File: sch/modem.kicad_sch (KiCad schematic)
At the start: 35 parts, among them J10 20579-001E, J11 732511150, J12 732511150, J13 732511150, J14 732511150, J6 20579-001E, J7 20579-001E, J8 20579-001E, J9 M.2_Socket_B, P1 SF72S006VBDR2500, Q3 NX3008NBKW_115

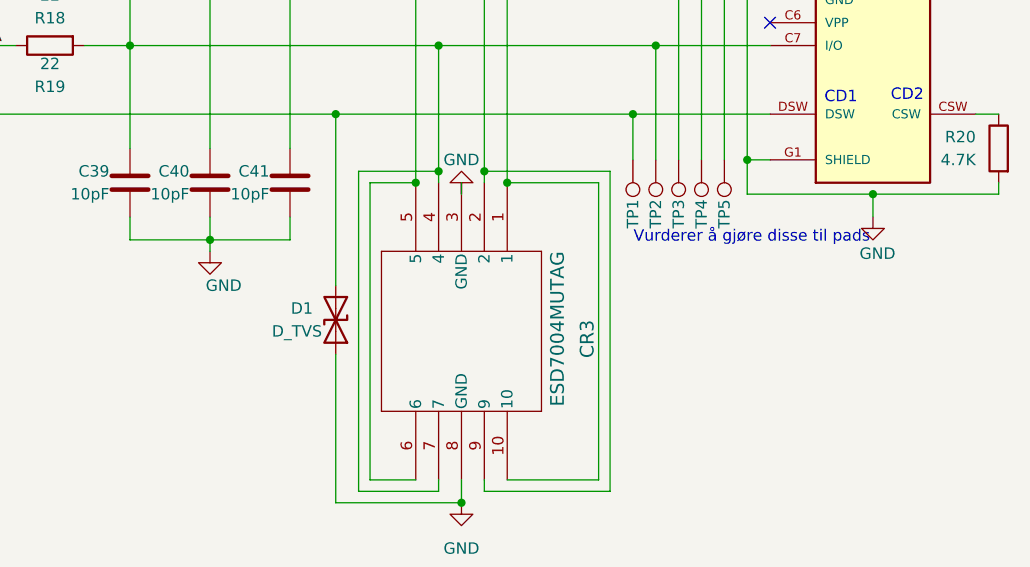
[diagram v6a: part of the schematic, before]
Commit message: partnumber, manufaturerer and description cleanup completed
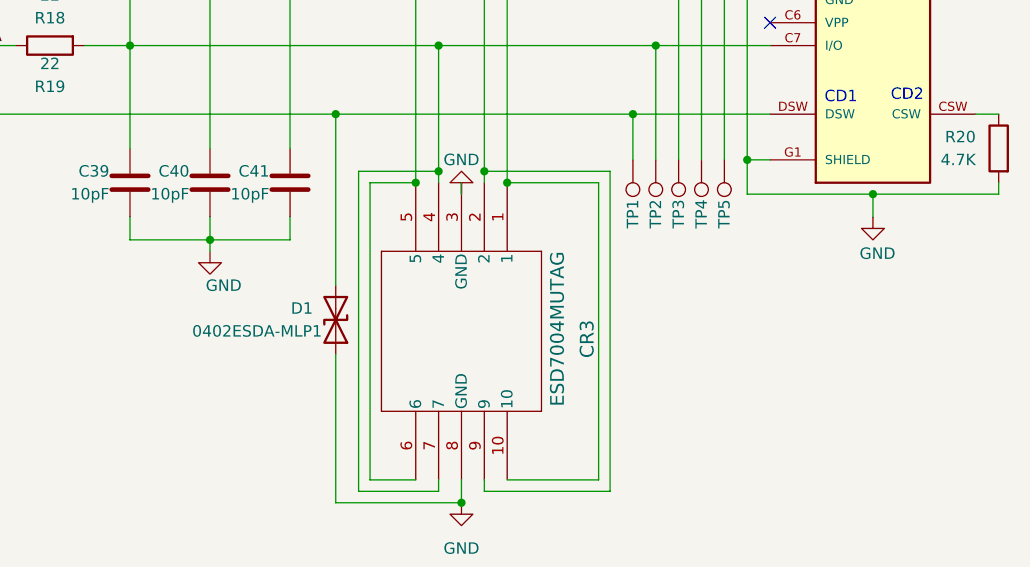
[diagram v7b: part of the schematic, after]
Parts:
- CR3: MPN (none) -> ESD7004MUTAG
- D1: value D_TVS -> 0402ESDA-MLP1
- J10: Description_1 1 POS Vertical SMD Coaxial connector M.2 industry standard 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 -> (none); MANUFACTURER I-PEX -> (none); MP 20579-001E -> (none); MPN (none) -> 20579-001E; Manufacturer (none) -> I-PEX
- J11, J12, J13, J14: Description_1 Right Angle 50Ohms Edge Mount SMA Connector, jack, Solder T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 -> (none); MANUFACTURER_PART_NUMBER 732511150 -> (none); MF Molex -> (none); MPN (none) -> 732511150; Manufacturer (none) -> Molex
- J6, J7, J8: MANUFACTURER I-PEX -> (none); MP 20579-001E -> (none); MPN (none) -> 20579-001E; Manufacturer (none) -> I-PEX
- J9: Description_1 M.2 0.5PITCH 3.2H KEY B 15Uinch AU, M.2 Connectors | TE Con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 -> (none); MANUFACTURER TE Connectivity -> (none); MP 2199119-3 -> (none); MPN (none) -> 2199119-3; Manufacturer (none) -> TE Connectivity
- MP5: Description_1 Round Standoff Threaded M2x0.4 Steel 0.118 (3.00mm) - -> (none); MF Würth Elektronik -> (none); MP 9774030243R -> (none); MPN (none) -> 9774030243R; Manufacturer  (none) -> Würth Elektronik
- MP6: Description_1 Round Standoff Threaded M2x0.4 Steel 0.118 (3.00mm) - -> (none); MF Würth Elektronik -> (none); MP 9774030243R -> (none); MPN (none) -> 9774030243R; Manufacturer (none) -> Würth Elektronik
- P1: Description_1 8 (6 + 2) Position Card Connector NANO SIM Surface Mount, R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 -> (none); MANUFACTURER JAE -> (none); MP SF72S006VBAR2500 -> (none); MPN (none) -> SF72S006VBAR2500; Manufacturer (none) -> JAE
- Q3: Description_1 N-Channel 30 V 350mA (Ta) 260mW (Ta), 830mW (Tc) Surface Mo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 -> (none); MANUFACTURER Nexperia -> (none); MP NX3008NBKW,115 -> (none); MPN (none) -> NX3008NBKW,115; Manufacturer (none) -> Nexperia
- R20: Field5 RC0603FR-074K7L -> (none); MPN (none) -> RC0603FR-074K7L
- R22: MPN RMCF0603FT100K -> RC0603FR-07100KL
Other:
- note removed: "Vurderer å gjøre disse til pads"
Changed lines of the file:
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@@
 		)
 	)
-	(text "Vurderer å gjøre disse til pads"
-		(exclude_from_sim no)
-		(at 250.698 77.216 0)
-		(effects
-			(font
-				(size 1.27 1.27)
-			)
-		)
-	)
 	(text "Activity \nLED"
 		(exclude_from_sim no)
@@
 			)
 		)
-		(property "Description" ""
+		(property "Description" "8 (6 + 2) Position Card Connector NANO SIM Surface Mount, Right Angle Gold"
 			(at 257.81 55.88 0)
 			(effects
@@
 			)
 		)
-		(property "Description_1" "8 (6 + 2) Position Card Connector NANO SIM Surface Mount, Right Angle Gold"
-			(at 257.81 55.88 0)
-			(effects
-				(font
-					(size 1.27 1.27)
-				)
-				(justify bottom)
-				(hide yes)
-			)
-		)
 		(property "Package" "None"
 			(at 257.81 55.88 0)
@@
 			)
 		)
-		(property "MP" "SF72S006VBAR2500"
+		(property "MPN" "SF72S006VBAR2500"
 			(at 257.81 55.88 0)
 			(effects
@@
 			)
 		)
-		(property "MANUFACTURER" "JAE"
+		(property "Manufacturer" "JAE"
 			(at 257.81 55.88 0)
 			(effects
@@
 			)
 		)
-		(property "Description" ""
+		(property "Description" "1 POS Vertical SMD Coaxial connector M.2 industry standard with a mated height of 1.4 mm and support up to 12 GHz MHF 4L Receptacle"
 			(at 68.58 152.4 0)
 			(effects
@@
 			)
 		)
-		(property "MP" "20579-001E"
+		(property "MPN" "20579-001E"
 			(at 68.58 152.4 0)
 			(effects
@@
 			)
 		)
-		(property "MANUFACTURER" "I-PEX"
+		(property "Manufacturer" "I-PEX"
 			(at 68.58 152.4 0)
 			(effects
@@
 			)
 		)
-		(property "Description" ""
-			(at 68.58 162.56 0)
-			(effects
-				(font
-					(size 1.27 1.27)
-				)
-				(hide yes)
-			)
-		)
-		(property "MF" "Molex"
+		(property "Description" "Right Angle 50Ohms Edge Mount SMA Connector, jack, Solder Termination | Molex Incorporated 73251-1150"
 			(at 68.58 162.56 0)
 			(effects
@@
 					(size 1.27 1.27)
 				)
-				(justify bottom)
 				(hide yes)
 			)
 		)
-		(property "Description_1" "Right Angle 50Ohms Edge Mount SMA Connector, jack, Solder Termination | Molex Incorporated 73251-1150"
+		(property "Manufacturer" "Molex"
 			(at 68.58 162.56 0)
 			(effects
@@
 			)
 		)
-		(property "MANUFACTURER_PART_NUMBER" "732511150"
+		(property "MPN" "732511150"
 			(at 68.58 162.56 0)
 			(effects
@@
 			)
 		)
-		(property "Description" ""
+		(property "Description" "1 POS Vertical SMD Coaxial connector M.2 industry standard with a mated height of 1.4 mm and support up to 12 GHz MHF 4L Receptacle"
 			(at 101.6 152.4 0)
 			(effects
@@
 			)
 		)
-		(property "MP" "20579-001E"
+		(property "MPN" "20579-001E"
 			(at 101.6 152.4 0)
 			(effects
@@
 			)
 		)
-		(property "MANUFACTURER" "I-PEX"
+		(property "Manufacturer" "I-PEX"
 			(at 101.6 152.4 0)
 			(effects
@@
 			)
 		)
-		(property "Description" ""
+		(property "Description" "Round Standoff Threaded M2x0.4 Steel 0.118 (3.00mm) -"
 			(at 251.46 133.35 0)
 			(effects
@@
 			)
 		)
-		(property "MF" "Würth Elektronik"
+		(property "Manufacturer " "Würth Elektronik"
 			(at 251.46 133.35 0)
 			(effects
@@
 			)
 		)
-		(property "MP" "9774030243R"
+		(property "MPN" "9774030243R"
 			(at 251.46 133.35 0)
 			(effects
@@
 			)
 		)
-		(property "Description_1" "Round Standoff Threaded M2x0.4 Steel 0.118 (3.00mm) -"
-			(at 251.46 133.35 0)
-			(effects
-				(font
-					(size 1.27 1.27)
-				)
-				(justify bottom)
-				(hide yes)
-			)
-		)
 		(pin "1"
 		)
@@
 			)
 		)
-		(property "Description" ""
-			(at 85.09 162.56 0)
-			(effects
-				(font
-					(size 1.27 1.27)
-				)
-				(hide yes)
-			)
-		)
-		(property "MF" "Molex"
+		(property "Description" "Right Angle 50Ohms Edge Mount SMA Connector, jack, Solder Termination | Molex Incorporated 73251-1150"
 			(at 85.09 162.56 0)
 			(effects
@@
 					(size 1.27 1.27)
 				)
-				(justify bottom)
 				(hide yes)
 			)
 		)
-		(property "Description_1" "Right Angle 50Ohms Edge Mount SMA Connector, jack, Solder Termination | Molex Incorporated 73251-1150"
+		(property "Manufacturer" "Molex"
 			(at 85.09 162.56 0)
 			(effects
@@
 			)
 		)
-		(property "MANUFACTURER_PART_NUMBER" "732511150"
+		(property "MPN" "732511150"
 			(at 85.09 162.56 0)
 			(effects
@@
 			)
 		)
-		(property "Description" ""
+		(property "Description" "1 POS Vertical SMD Coaxial connector M.2 industry standard with a mated height of 1.4 mm and support up to 12 GHz MHF 4L Receptacle"
 			(at 85.09 152.4 0)
 			(effects
@@
 			)
 		)
-		(property "MP" "20579-001E"
+		(property "MPN" "20579-001E"
 			(at 85.09 152.4 0)
 			(effects
@@
 			)
 		)
-		(property "MANUFACTURER" "I-PEX"
+		(property "Manufacturer" "I-PEX"
 			(at 85.09 152.4 0)
 			(effects
@@
 			)
 		)
-		(property "Description" ""
+		(property "Description" "Right Angle 50Ohms Edge Mount SMA Connector, jack, Solder Termination | Molex Incorporated 73251-1150"
 			(at 101.6 162.56 0)
 			(effects
@@
 			)
 		)
-		(property "MF" "Molex"
-			(at 101.6 162.56 0)
-			(effects
-				(font
-					(size 1.27 1.27)
-				)
-				(justify bottom)
-				(hide yes)
-			)
-		)
-		(property "Description_1" "Right Angle 50Ohms Edge Mount SMA Connector, jack, Solder Termination | Molex Incorporated 73251-1150"
+		(property "Manufacturer" "Molex"
 			(at 101.6 162.56 0)
 			(effects
@@
 			)
 		)
-		(property "MANUFACTURER_PART_NUMBER" "732511150"
+		(property "MPN" "732511150"
 			(at 101.6 162.56 0)
 			(effects
@@
 			)
 		)
-		(property "Value" "D_TVS"
+		(property "Value" "0402ESDA-MLP1"
 			(at 202.946 87.63 90)
 			(effects
@@
 			)
 		)
-		(property "Description" ""
+		(property "Description" "Round Standoff Threaded M2x0.4 Steel 0.118 (3.00mm) -"
 			(at 251.46 140.97 0)
 			(effects
@@
 			)
 		)
-		(property "MF" "Würth Elektronik"
+		(property "Manufacturer" "Würth Elektronik"
 			(at 251.46 140.97 0)
 			(effects
@@
 			)
 		)
-		(property "MP" "9774030243R"
+		(property "MPN" "9774030243R"
 			(at 251.46 140.97 0)
 			(effects
@@
 			)
 		)
-		(property "Description_1" "Round Standoff Threaded M2x0.4 Steel 0.118 (3.00mm) -"
-			(at 251.46 140.97 0)
-			(effects
-				(font
-					(size 1.27 1.27)
-				)
-				(justify bottom)
-				(hide yes)
-			)
-		)
 		(pin "1"
 		)
@@
 			)
 		)
-		(property "MPN" "RMCF0603FT100K"
+		(property "MPN" "RC0603FR-07100KL"
 			(at 40.64 118.11 0)
 			(effects
@@
 			)
 		)
-		(property "Description" ""
+		(property "Description" "Right Angle 50Ohms Edge Mount SMA Connector, jack, Solder Termination | Molex Incorporated 73251-1150"
 			(at 118.11 162.56 0)
 			(effects
@@
 			)
 		)
-		(property "MF" "Molex"
-			(at 118.11 162.56 0)
-			(effects
-				(font
-					(size 1.27 1.27)
-				)
-				(justify bottom)
-				(hide yes)
-			)
-		)
-		(property "Description_1" "Right Angle 50Ohms Edge Mount SMA Connector, jack, Solder Termination | Molex Incorporated 73251-1150"
+		(property "Manufacturer" "Molex"
 			(at 118.11 162.56 0)
 			(effects
@@
 			)
 		)
-		(property "MANUFACTURER_PART_NUMBER" "732511150"
+		(property "MPN" "732511150"
 			(at 118.11 162.56 0)
 			(effects
@@
 			)
 		)
-		(property "Description" ""
+		(property "Description" "N-Channel 30 V 350mA (Ta) 260mW (Ta), 830mW (Tc) Surface Mount SOT-323"
 			(at 50.8 110.49 0)
 			(effects
@@
 			)
 		)
-		(property "Description_1" "N-Channel 30 V 350mA (Ta) 260mW (Ta), 830mW (Tc) Surface Mount SOT-323"
-			(at 50.8 110.49 0)
-			(effects
-				(font
-					(size 1.27 1.27)
-				)
-				(justify bottom)
-				(hide yes)
-			)
-		)
 		(property "Package" "SC-70-3 Nexperia USA Inc."
 			(at 50.8 110.49 0)
@@
 			)
 		)
-		(property "MP" "NX3008NBKW,115"
+		(property "MPN" "NX3008NBKW,115"
 			(at 50.8 110.49 0)
 			(effects
@@
 			)
 		)
-		(property "MANUFACTURER" "Nexperia"
+		(property "Manufacturer" "Nexperia"
 			(at 50.8 110.49 0)
 			(effects
@@
 			)
 		)
-		(property "Description" ""
+		(property "Description" "ESD Protection Diodes / TVS Diodes Low Capacitance ESD Protection Diode"
+			(at 219.71 71.12 0)
+			(effects
+				(font
+					(size 1.27 1.27)
+				)
+				(hide yes)
+			)
+		)
+		(property "MPN" "ESD7004MUTAG"
 			(at 219.71 71.12 0)
 			(effects
@@
 			)
 		)
-		(property "Description" ""
+		(property "Description" "1 POS Vertical SMD Coaxial connector M.2 industry standard with a mated height of 1.4 mm and support up to 12 GHz MHF 4L Receptacle"
 			(at 118.11 152.4 0)
 			(effects
@@
 			)
 		)
-		(property "MP" "20579-001E"
+		(property "MPN" "20579-001E"
 			(at 118.11 152.4 0)
 			(effects
@@
 			)
 		)
-		(property "Description_1" "1 POS Vertical SMD Coaxial connector M.2 industry standard with a mated height of 1.4 mm and support up to 12 GHz MHF 4L Receptacle"
+		(property "Description_1" ""
 			(at 118.11 152.4 0)
 			(effects
@@
 			)
 		)
-		(property "MANUFACTURER" "I-PEX"
+		(property "Manufacturer" "I-PEX"
 			(at 118.11 152.4 0)
 			(effects
@@
 			)
 		)
-		(property "Description" "M.2 Socket 3 Mechanical Key B"
+		(property "Description" "M.2 0.5PITCH 3.2H KEY B 15Uinch AU, M.2 Connectors | TE Connectivity 2199119-3"
 			(at 91.44 73.66 0)
 			(effects
@@
 			)
 		)
-		(property "MP" "2199119-3"
+		(property "MPN" "2199119-3"
 			(at 91.44 73.66 0)
 			(effects
@@
 			)
 		)
-		(property "Description_1" "M.2 0.5PITCH 3.2H KEY B 15Uinch AU, M.2 Connectors | TE Connectivity 2199119-3"
-			(at 91.44 73.66 0)
-			(effects
-				(font
-					(size 1.27 1.27)
-				)
-				(justify bottom)
-				(hide yes)
-			)
-		)
 		(property "Availability" "In Stock"
 			(at 91.44 73.66 0)
@@
 			)
 		)
-		(property "MANUFACTURER" "TE Connectivity"
+		(property "Manufacturer" "TE Connectivity"
 			(at 91.44 73.66 0)
 			(effects
@@
 			)
 		)
-		(property "Field5" "RC0603FR-074K7L"
+		(property "MPN" "RC0603FR-074K7L"
 			(at 278.13 67.31 0)
 			(effects

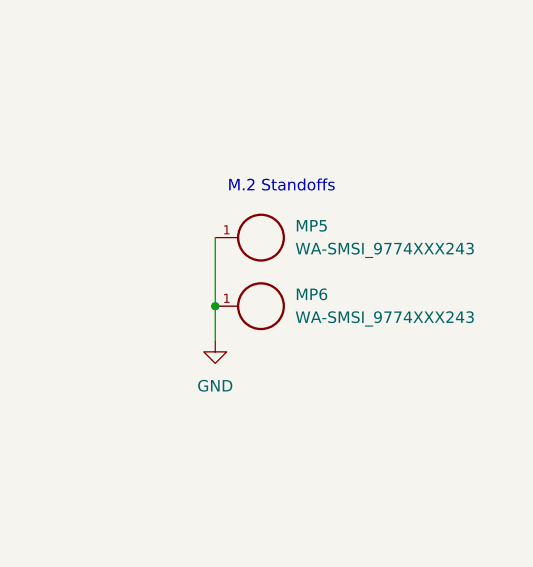
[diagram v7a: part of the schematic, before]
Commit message: update licence to CERN-OHL-S
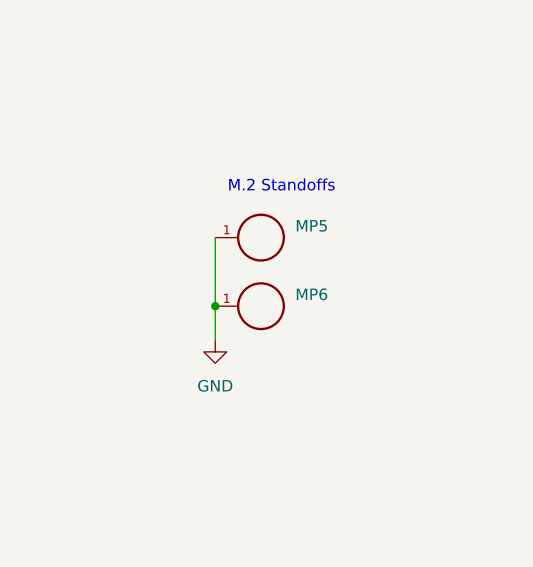
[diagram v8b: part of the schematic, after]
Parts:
- MP5, MP6: value WA-SMSI_9774XXX243 -> M2 x 3mm; VALUE M2 x 3mm -> (none)
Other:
- title: Modem -> Audiograb
